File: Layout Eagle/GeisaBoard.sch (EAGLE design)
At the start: 21 parts, among them IC1 4052N, IC2 4052N, U1 328P

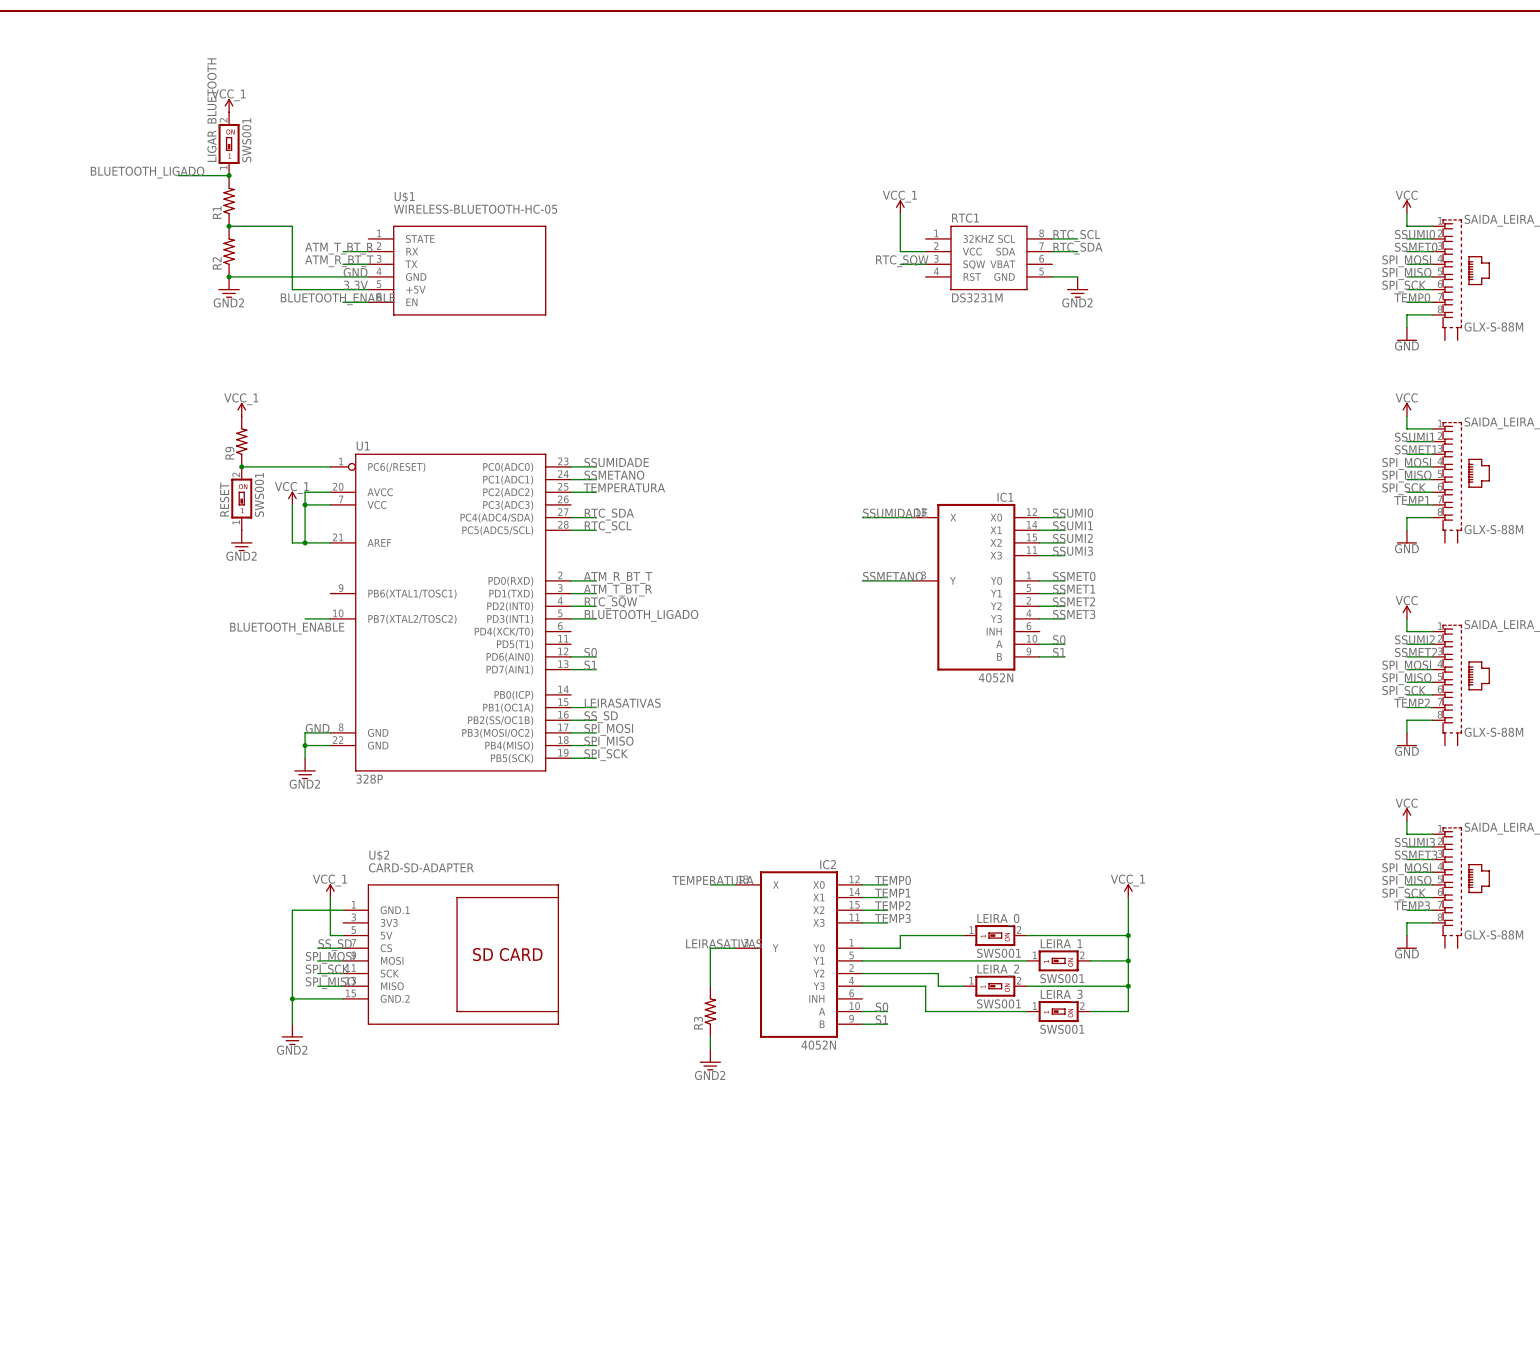
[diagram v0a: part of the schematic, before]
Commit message: Layout atualizado da placa
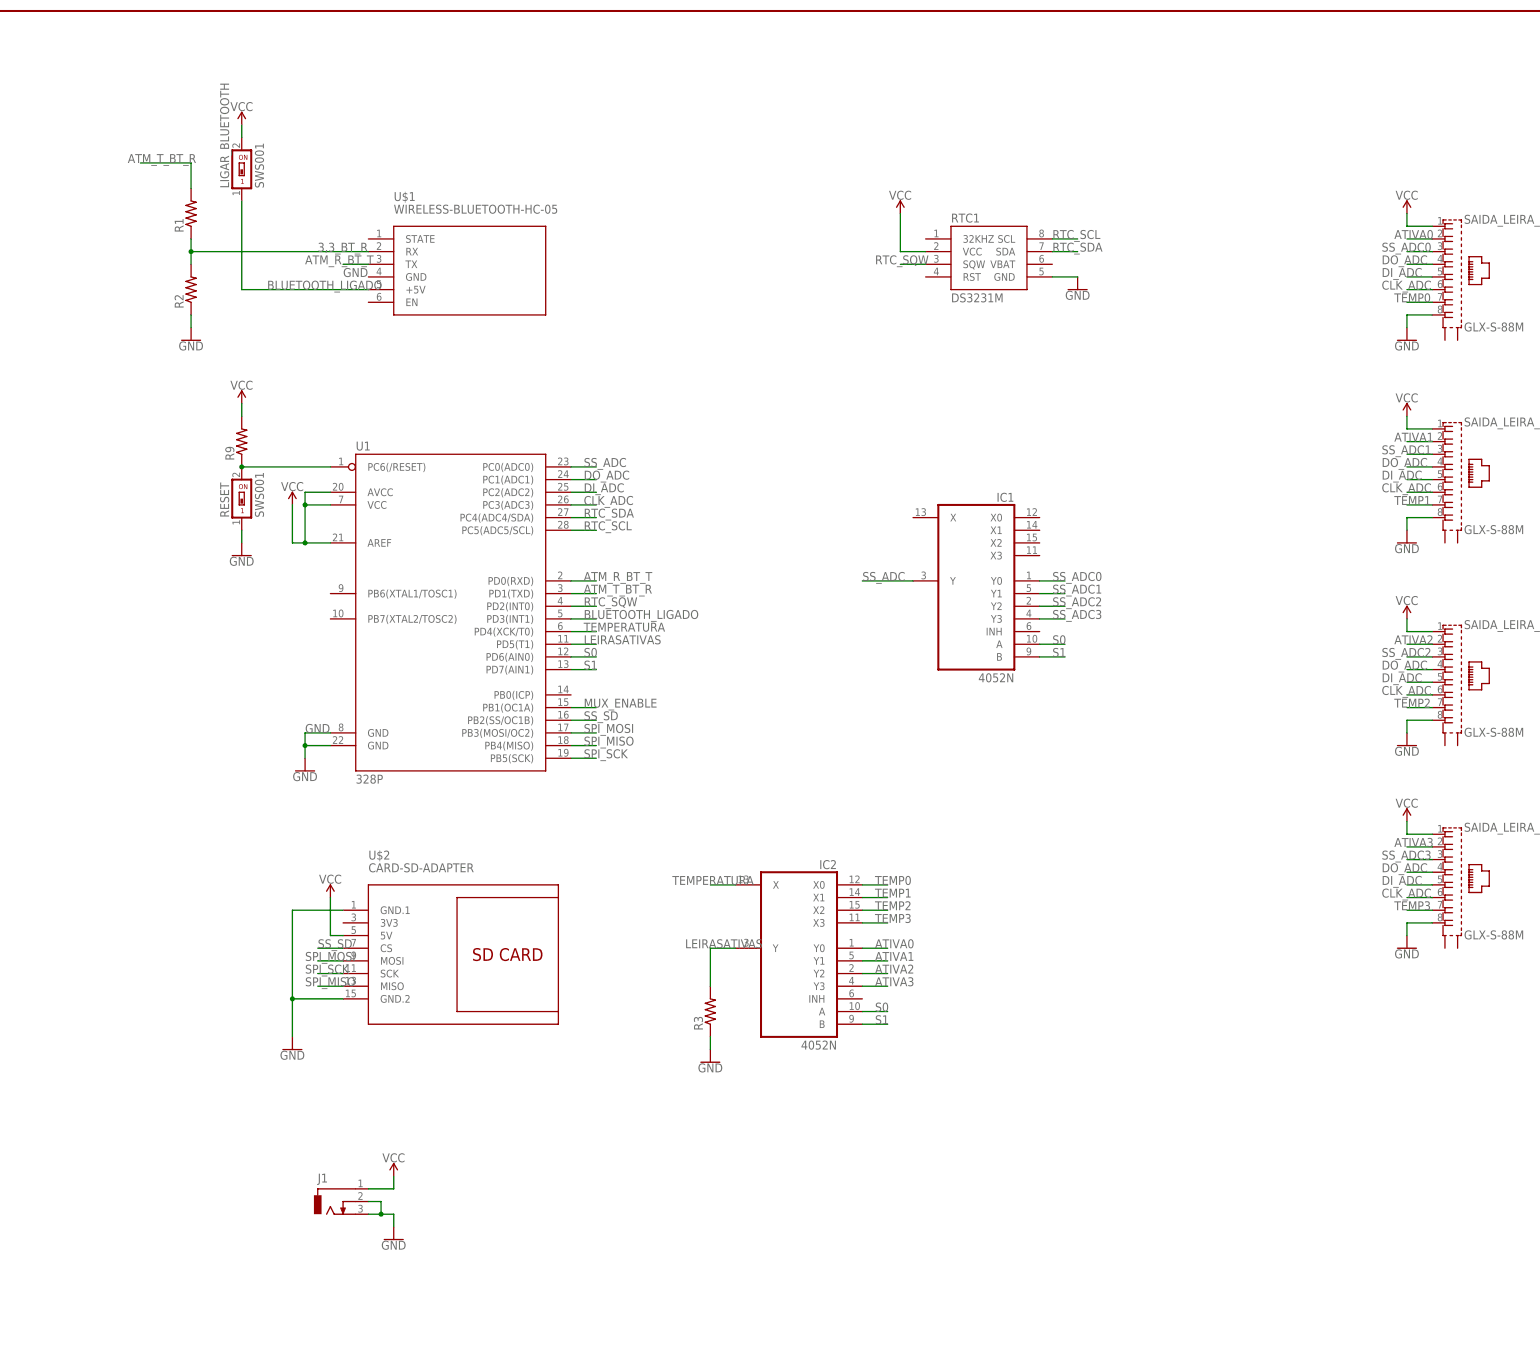
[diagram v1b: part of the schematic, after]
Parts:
- removed LEIRA_0, LEIRA_1, LEIRA_2, LEIRA_3: SWS001, smd-special:SWS001
- added J1: (no value), con-jack:DCJ0303
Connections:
- net SSMET0 renamed SS_ADC0
- net SSMET1 renamed SS_ADC1
- net SSMET2 renamed SS_ADC2
- net SSMET3 renamed SS_ADC3
- removed net 3.3V: R1.1, R2.2, U$1.+5V
- removed net BLUETOOTH_ENABLE: U$1.EN, U1.PB7(XTAL2/TOSC2)
- removed net N$1: IC2A.Y1, LEIRA_1.1
- removed net N$2: IC2A.Y0, LEIRA_0.1
- removed net N$3: IC2A.Y2, LEIRA_2.1
- removed net N$4: IC2A.Y3, LEIRA_3.1
- removed net SSMETANO: IC1A.Y, U1.PC1(ADC1)
- removed net SSUMI0: IC1A.X0, SAIDA_LEIRA_0.2
- removed net SSUMI1: IC1A.X1, SAIDA_LEIRA_1.2
- removed net SSUMI2: IC1A.X2, SAIDA_LEIRA_2.2
- removed net SSUMI3: IC1A.X3, SAIDA_LEIRA_3.2
- removed net SSUMIDADE: IC1A.X, U1.PC0(ADC0)
- removed net VCC_1: LEIRA_0.2, LEIRA_1.2, LEIRA_2.2, LEIRA_3.2, LIGAR_BLUETOOTH.2, R9.2, RTC1.VCC, U$2.5V, U1.AREF, U1.AVCC, U1.VCC
- new net 3,3_BT_R: R1.1, R2.2, U$1.RX
- new net ATIVA0: IC2A.Y0, SAIDA_LEIRA_0.2
- new net ATIVA1: IC2A.Y1, SAIDA_LEIRA_1.2
- new net ATIVA2: IC2A.Y2, SAIDA_LEIRA_2.2
- new net ATIVA3: IC2A.Y3, SAIDA_LEIRA_3.2
- new net CLK_ADC: SAIDA_LEIRA_0.6, SAIDA_LEIRA_1.6, SAIDA_LEIRA_2.6, SAIDA_LEIRA_3.6, U1.PC3(ADC3)
- new net DI_ADC: SAIDA_LEIRA_0.5, SAIDA_LEIRA_1.5, SAIDA_LEIRA_2.5, SAIDA_LEIRA_3.5, U1.PC2(ADC2)
- new net DO_ADC: SAIDA_LEIRA_0.4, SAIDA_LEIRA_1.4, SAIDA_LEIRA_2.4, SAIDA_LEIRA_3.4, U1.PC1(ADC1)
- new net MUX_ENABLE: U1.PB1(OC1A)
- new net SS_ADC: IC1A.Y, U1.PC0(ADC0)
- net ATM_T_BT_R: now also R1.2; no longer U$1.RX
- net BLUETOOTH_LIGADO: now also U$1.+5V; no longer R1.2
- net GND: now also J1.2, J1.3; no longer U$1.GND
- net LEIRASATIVAS: now also U1.PD5(T1); no longer U1.PB1(OC1A)
- net SPI_MISO: no longer SAIDA_LEIRA_0.5, SAIDA_LEIRA_1.5, SAIDA_LEIRA_2.5, SAIDA_LEIRA_3.5
- net SPI_MOSI: no longer SAIDA_LEIRA_0.4, SAIDA_LEIRA_1.4, SAIDA_LEIRA_2.4, SAIDA_LEIRA_3.4
- net SPI_SCK: no longer SAIDA_LEIRA_0.6, SAIDA_LEIRA_1.6, SAIDA_LEIRA_2.6, SAIDA_LEIRA_3.6
- net TEMPERATURA: now also U1.PD4(XCK/T0); no longer U1.PC2(ADC2)
- net VCC: now also J1.1, LIGAR_BLUETOOTH.2, R9.2, RTC1.VCC, U$2.5V, U1.AREF, U1.AVCC, U1.VCC
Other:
- moved on the sheet: LIGAR_BLUETOOTH, R1, R2

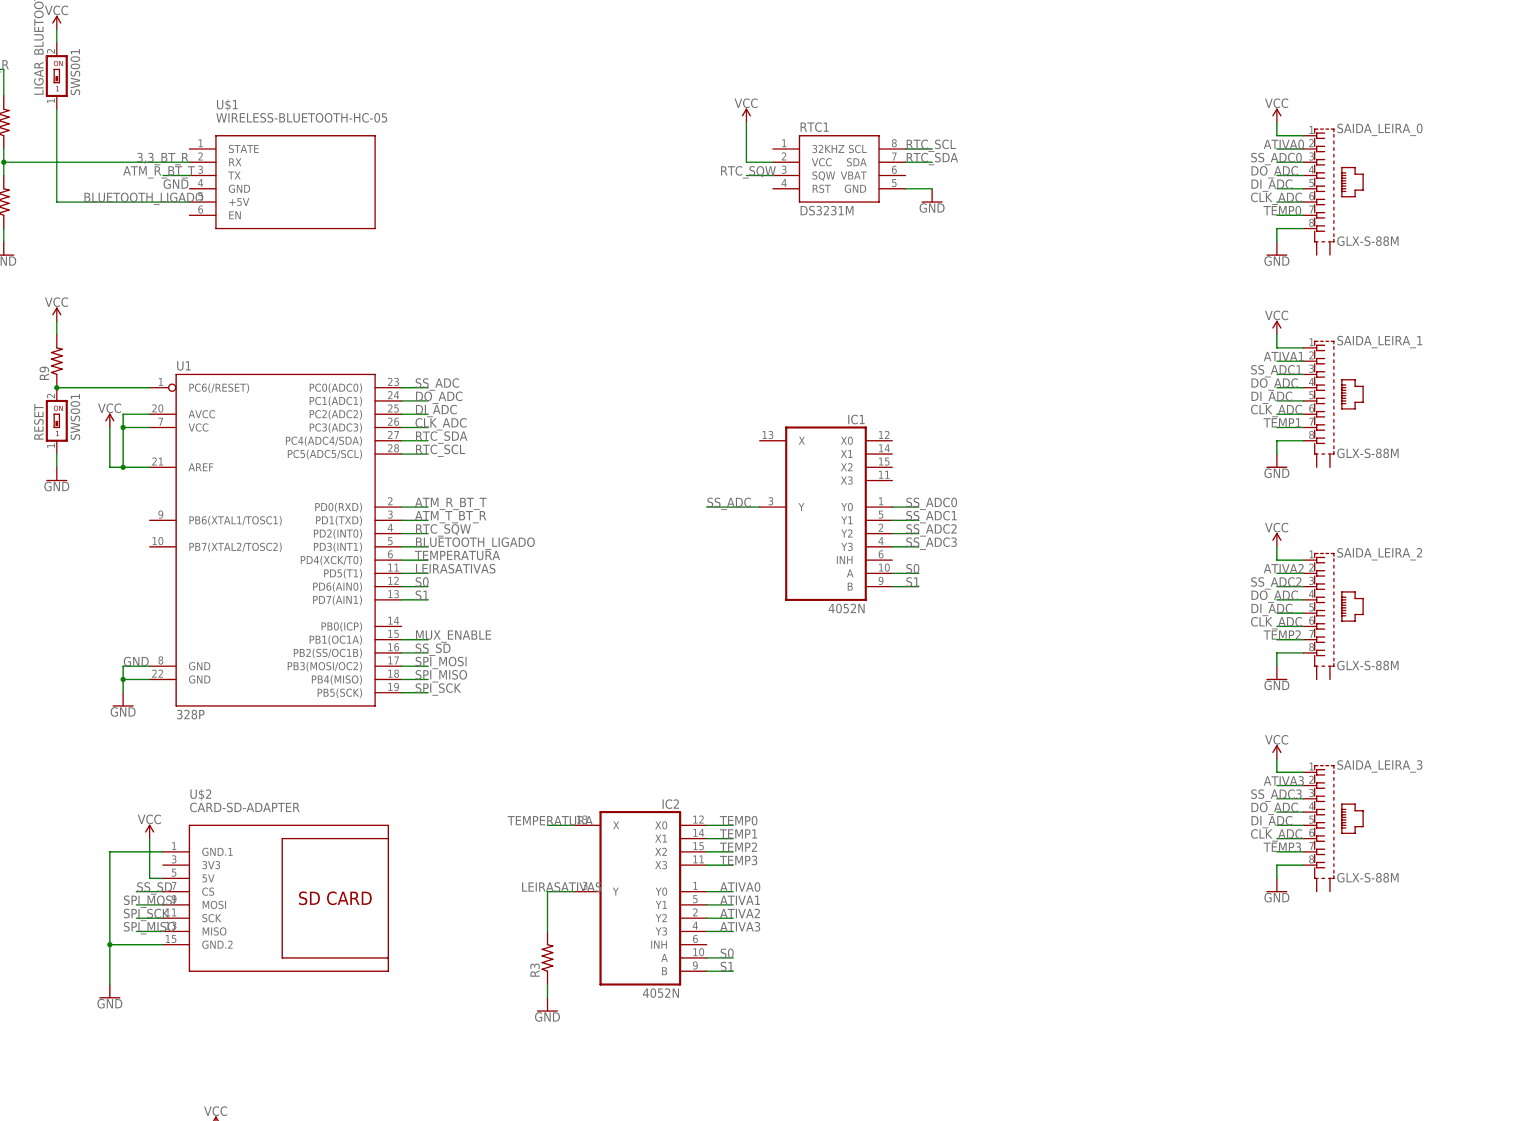
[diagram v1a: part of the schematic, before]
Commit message: Esquemático corrigido
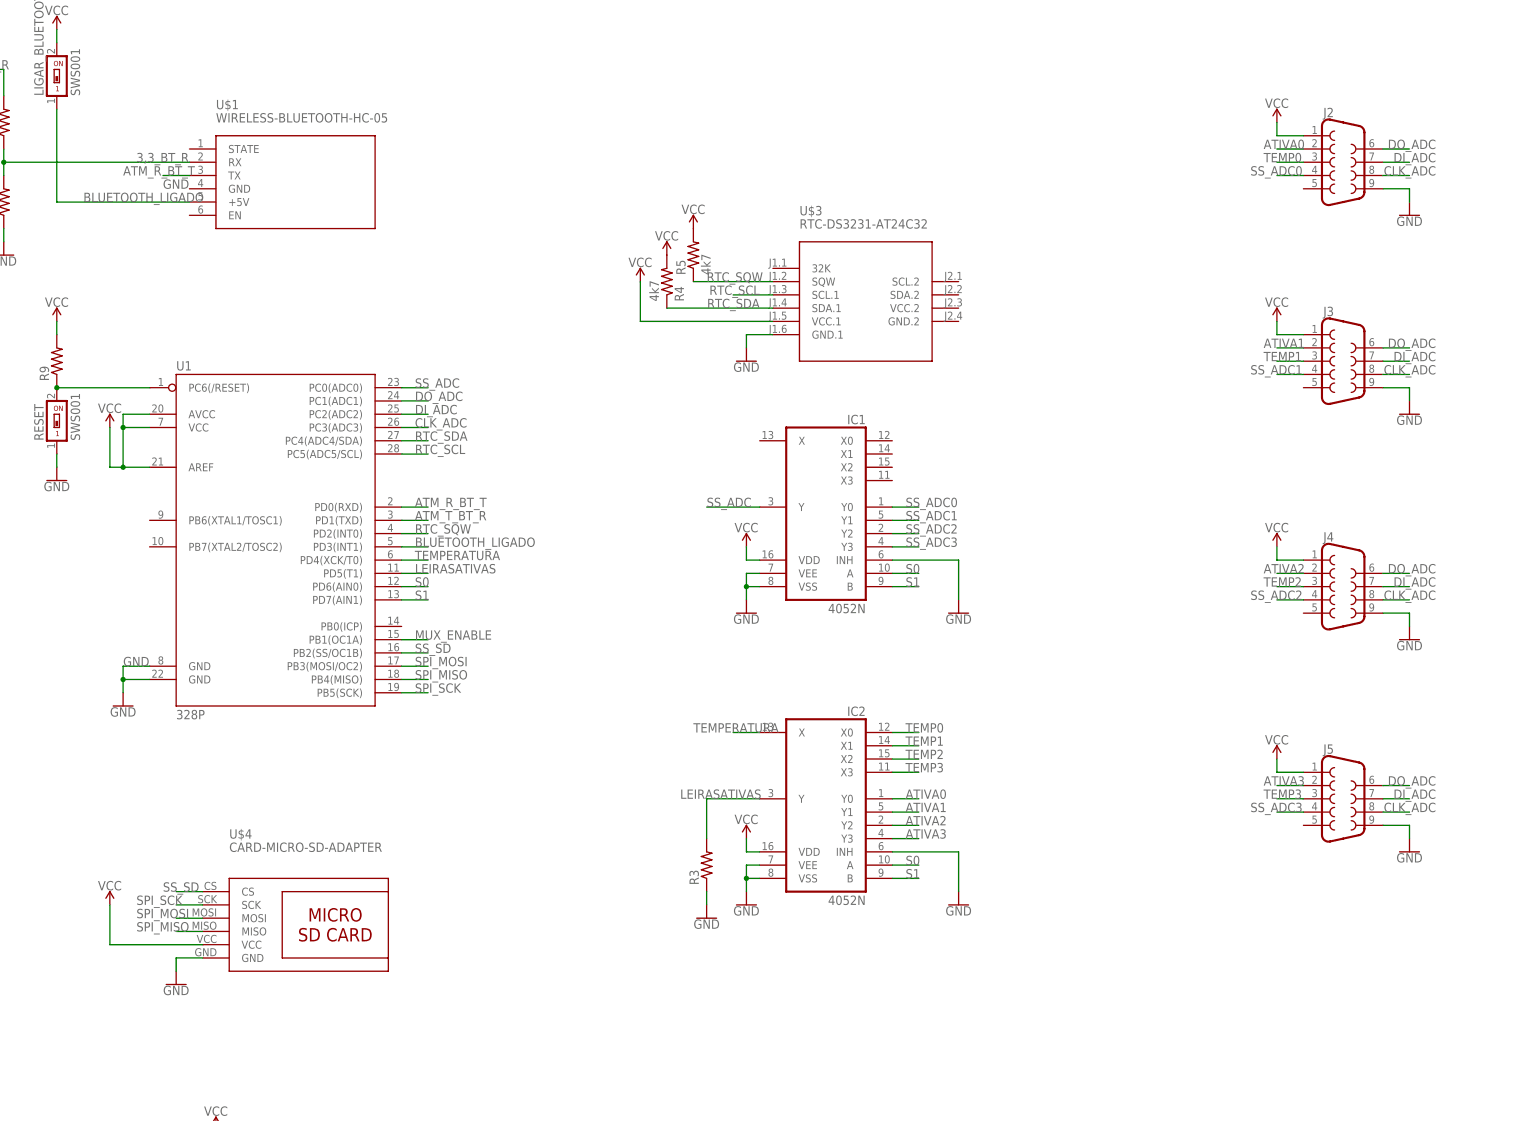
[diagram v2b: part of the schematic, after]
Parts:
- removed RTC1: DS3231M, SparkFun-Clocks:DS3231M
- removed SAIDA_LEIRA_0, SAIDA_LEIRA_1, SAIDA_LEIRA_2, SAIDA_LEIRA_3: GLX-S-88M, con-kycon:GLX-S-88M
- removed U$2: CARD-SD-ADAPTER, diy-modules:CARD-SD-ADAPTER
- added J2, J3, J4, J5: (no value), SparkFun-Connectors:DB9FEMALE
- added R4, R5: 4k7, rcl:R-US_0204/7
- added U$3: RTC-DS3231-AT24C32, diy-modules:RTC-DS3231-AT24C32
- added U$4: CARD-MICRO-SD-ADAPTER, Geisa:CARD-MICRO-SD-ADAPTER
- IC1, IC2: device 40xx:4052N -> Geisa:4052N
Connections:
- net ATIVA0: now also IC2.Y0, J2.2; no longer IC2A.Y0, SAIDA_LEIRA_0.2
- net ATIVA1: now also IC2.Y1, J3.2; no longer IC2A.Y1, SAIDA_LEIRA_1.2
- net ATIVA2: now also IC2.Y2, J4.2; no longer IC2A.Y2, SAIDA_LEIRA_2.2
- net ATIVA3: now also IC2.Y3, J5.2; no longer IC2A.Y3, SAIDA_LEIRA_3.2
- net CLK_ADC: now also J2.8, J3.8, J4.8, J5.8; no longer SAIDA_LEIRA_0.6, SAIDA_LEIRA_1.6, SAIDA_LEIRA_2.6, SAIDA_LEIRA_3.6
- net DI_ADC: now also J2.7, J3.7, J4.7, J5.7; no longer SAIDA_LEIRA_0.5, SAIDA_LEIRA_1.5, SAIDA_LEIRA_2.5, SAIDA_LEIRA_3.5
- net DO_ADC: now also J2.6, J3.6, J4.6, J5.6; no longer SAIDA_LEIRA_0.4, SAIDA_LEIRA_1.4, SAIDA_LEIRA_2.4, SAIDA_LEIRA_3.4
- net GND: now also IC1.INH, IC1.VEE, IC1.VSS, IC2.INH, IC2.VEE, IC2.VSS, J2.9, J3.9, J4.9, J5.9, U$3.GND.1, U$4.GND; no longer RTC1.GND, SAIDA_LEIRA_0.8, SAIDA_LEIRA_1.8, SAIDA_LEIRA_2.8, SAIDA_LEIRA_3.8, U$2.GND.1, U$2.GND.2
- net LEIRASATIVAS: now also IC2.Y; no longer IC2A.Y
- net RTC_SCL: now also U$3.SCL.1; no longer RTC1.SCL
- net RTC_SDA: now also R4.1, U$3.SDA.1; no longer RTC1.SDA
- net RTC_SQW: now also R5.1, U$3.SQW; no longer RTC1.SQW
- net S0: now also IC1.A, IC2.A; no longer IC1A.A, IC2A.A
- net S1: now also IC1.B, IC2.B; no longer IC1A.B, IC2A.B
- net SPI_MISO: now also U$4.MISO; no longer U$2.MISO
- net SPI_MOSI: now also U$4.MOSI; no longer U$2.MOSI
- net SPI_SCK: now also U$4.SCK; no longer U$2.SCK
- net SS_ADC: now also IC1.Y; no longer IC1A.Y
- net SS_ADC0: now also IC1.Y0, J2.4; no longer IC1A.Y0, SAIDA_LEIRA_0.3
- net SS_ADC1: now also IC1.Y1, J3.4; no longer IC1A.Y1, SAIDA_LEIRA_1.3
- net SS_ADC2: now also IC1.Y2, J4.4; no longer IC1A.Y2, SAIDA_LEIRA_2.3
- net SS_ADC3: now also IC1.Y3, J5.4; no longer IC1A.Y3, SAIDA_LEIRA_3.3
- net SS_SD: now also U$4.CS; no longer U$2.CS
- net TEMP0: now also IC2.X0, J2.3; no longer IC2A.X0, SAIDA_LEIRA_0.7
- net TEMP1: now also IC2.X1, J3.3; no longer IC2A.X1, SAIDA_LEIRA_1.7
- net TEMP2: now also IC2.X2, J4.3; no longer IC2A.X2, SAIDA_LEIRA_2.7
- net TEMP3: now also IC2.X3, J5.3; no longer IC2A.X3, SAIDA_LEIRA_3.7
- net TEMPERATURA: now also IC2.X; no longer IC2A.X
- net VCC: now also IC1.VDD, IC2.VDD, J2.1, J3.1, J4.1, J5.1, R4.2, R5.2, U$3.VCC.1, U$4.VCC; no longer RTC1.VCC, SAIDA_LEIRA_0.1, SAIDA_LEIRA_1.1, SAIDA_LEIRA_2.1, SAIDA_LEIRA_3.1, U$2.5V
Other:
- moved on the sheet: R3
